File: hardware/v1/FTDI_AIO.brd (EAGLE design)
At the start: 49.5 x 49.5 mm, 45 parts, among them IC1 MCP1702-3.3, IC2 FT232RL, X1 ISP, X2 USB-A-H, X3 UART

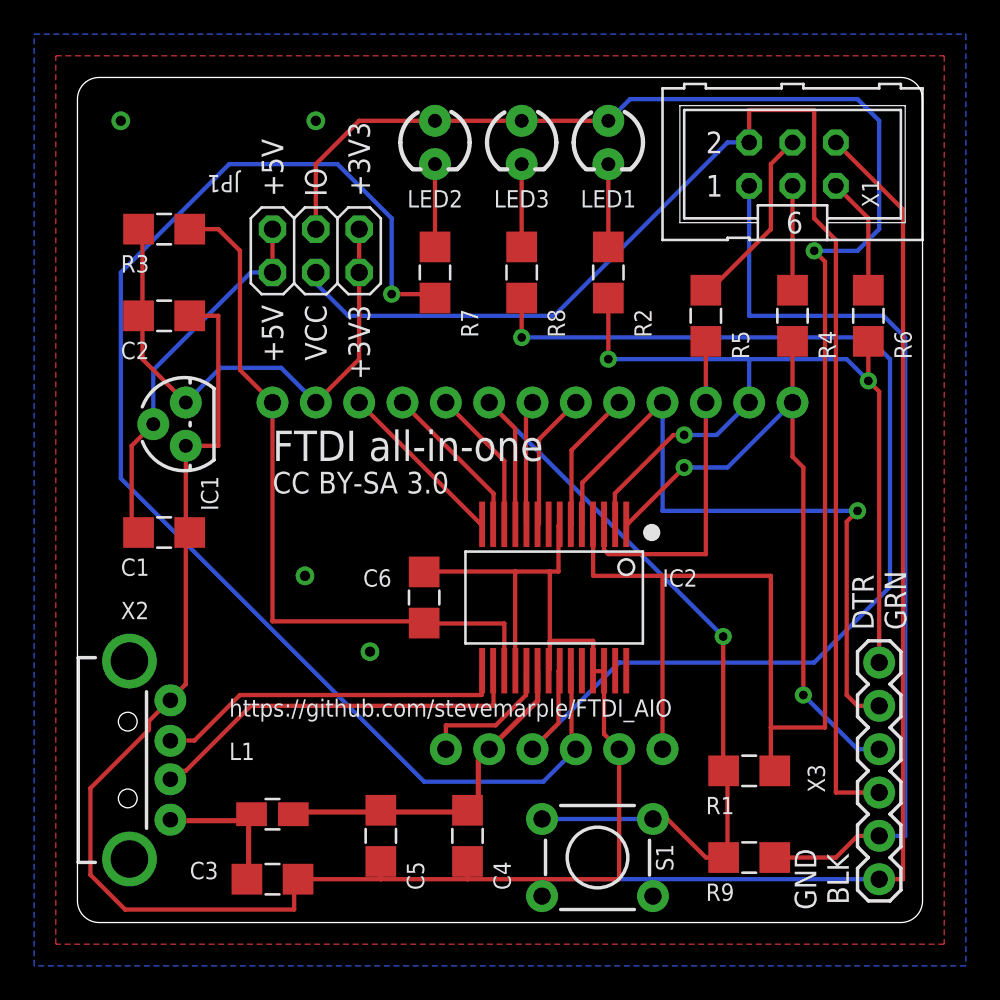
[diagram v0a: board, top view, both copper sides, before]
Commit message: Minor track and via changes.
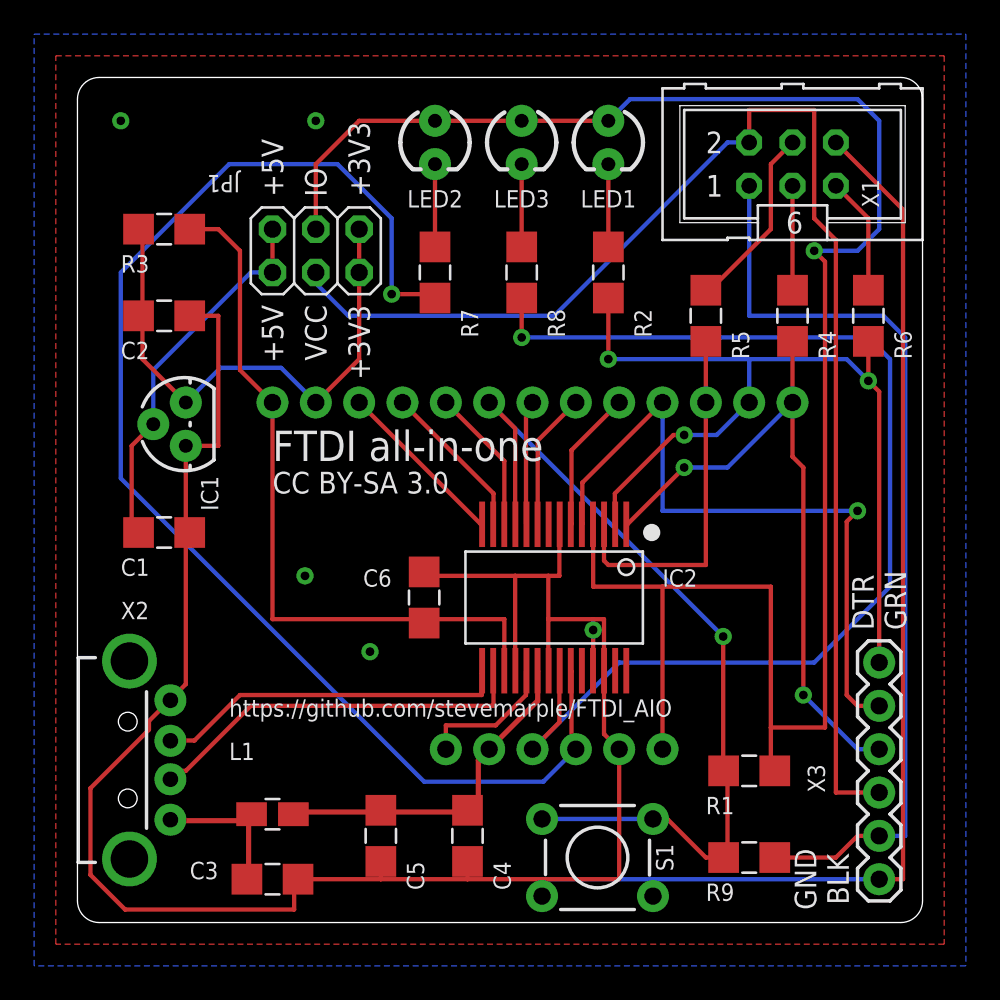
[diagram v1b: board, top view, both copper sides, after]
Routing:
- net GND: track 183.7 -> 188.1 mm, vias 4 -> 5
- net RTS: track 20.0 -> 21.3 mm
- net VCC: track 116.3 -> 115.6 mm
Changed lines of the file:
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@@
 <wire x1="46.99" y1="2.54" x2="48.387" y2="2.54" width="0.254" layer="1"/>
 <wire x1="6.477" y1="35.56" x2="6.579" y2="35.56" width="0.254" layer="1"/>
-<wire x1="28.194" y1="20.574" x2="27.686" y2="20.574" width="0.254" layer="1"/>
-<wire x1="27.686" y1="20.574" x2="25.654" y2="20.574" width="0.254" layer="1"/>
-<wire x1="25.654" y1="20.574" x2="20.32" y2="20.574" width="0.254" layer="1"/>
-<wire x1="28.194" y1="23.241" x2="28.194" y2="20.574" width="0.254" layer="1"/>
-<wire x1="20.32" y1="20.574" x2="20.32" y2="20.549" width="0.254" layer="1"/>
-<wire x1="28.194" y1="23.241" x2="28.265" y2="23.341" width="0.254" layer="1"/>
-<wire x1="25.654" y1="20.574" x2="25.654" y2="14.859" width="0.254" layer="1"/>
+<wire x1="28.2448" y1="20.32" x2="27.5971" y2="20.32" width="0.254" layer="1"/>
+<wire x1="27.5971" y1="20.32" x2="25.654" y2="20.32" width="0.254" layer="1"/>
+<wire x1="25.654" y1="20.32" x2="20.32" y2="20.32" width="0.254" layer="1"/>
+<wire x1="28.2448" y1="23.241" x2="28.2448" y2="20.32" width="0.254" layer="1"/>
+<wire x1="20.32" y1="20.32" x2="20.32" y2="20.549" width="0.254" layer="1"/>
+<wire x1="28.2448" y1="23.241" x2="28.265" y2="23.341" width="0.254" layer="1"/>
+<wire x1="25.654" y1="20.32" x2="25.654" y2="14.859" width="0.254" layer="1"/>
 <wire x1="25.654" y1="14.859" x2="25.665" y2="14.759" width="0.254" layer="1"/>
-<wire x1="27.686" y1="20.574" x2="27.686" y2="16.51" width="0.254" layer="1"/>
-<wire x1="27.686" y1="16.51" x2="27.686" y2="14.859" width="0.254" layer="1"/>
-<wire x1="27.686" y1="14.859" x2="27.615" y2="14.759" width="0.254" layer="1"/>
-<wire x1="30.861" y1="14.732" x2="30.226" y2="14.732" width="0.254" layer="1"/>
+<wire x1="27.5971" y1="20.32" x2="27.5971" y2="17.78" width="0.254" layer="1"/>
+<wire x1="27.5971" y1="17.78" x2="27.5971" y2="14.859" width="0.254" layer="1"/>
+<wire x1="27.5971" y1="14.859" x2="27.615" y2="14.759" width="0.254" layer="1"/>
 <wire x1="30.226" y1="14.732" x2="30.215" y2="14.759" width="0.254" layer="1"/>
 <wire x1="30.861" y1="14.732" x2="30.865" y2="14.759" width="0.254" layer="1"/>
@@
 <wire x1="31.75" y1="10.16" x2="30.861" y2="11.049" width="0.254" layer="1"/>
 <wire x1="30.861" y1="14.605" x2="30.865" y2="14.759" width="0.254" layer="1"/>
-<wire x1="30.226" y1="16.51" x2="27.686" y2="16.51" width="0.254" layer="1"/>
-<wire x1="30.226" y1="14.859" x2="30.226" y2="16.51" width="0.254" layer="1"/>
+<wire x1="30.226" y1="17.78" x2="27.5971" y2="17.78" width="0.254" layer="1"/>
+<wire x1="30.226" y1="14.859" x2="30.226" y2="17.78" width="0.254" layer="1"/>
 <wire x1="30.226" y1="14.859" x2="30.215" y2="14.759" width="0.254" layer="1"/>
 <wire x1="4.191" y1="11.811" x2="5.334" y2="12.954" width="0.254" layer="1"/>
@@
 <vertex x="-2.54" y="-2.54"/>
 </polygon>
-<via x="2.54" y="46.99" extent="1-16" drill="0.6"/>
-<via x="13.97" y="46.99" extent="1-16" drill="0.6"/>
-<via x="13.335" y="20.32" extent="1-16" drill="0.6"/>
-<via x="17.145" y="15.875" extent="1-16" drill="0.6"/>
+<via x="2.54" y="46.99" extent="1-16" drill="0.508"/>
+<via x="13.97" y="46.99" extent="1-16" drill="0.508"/>
+<via x="13.335" y="20.32" extent="1-16" drill="0.508"/>
+<via x="17.145" y="15.875" extent="1-16" drill="0.508"/>
+<via x="30.226" y="17.145" extent="1-16" drill="0.508"/>
+<wire x1="30.861" y1="14.732" x2="30.861" y2="17.78" width="0.254" layer="1"/>
+<wire x1="30.861" y1="17.78" x2="30.226" y2="17.78" width="0.254" layer="1"/>
 </signal>
 <signal name="TX">
@@
 <contactref element="JP1" pad="4"/>
 <contactref element="LED1" pad="A"/>
-<wire x1="40.64" y1="20.32" x2="40.64" y2="11.43" width="0.254" layer="1"/>
-<wire x1="34.29" y1="20.32" x2="40.64" y2="20.32" width="0.254" layer="1"/>
-<wire x1="34.29" y1="10.16" x2="34.29" y2="20.32" width="0.254" layer="1"/>
-<wire x1="30.226" y1="20.32" x2="30.226" y2="23.241" width="0.254" layer="1"/>
-<wire x1="34.29" y1="20.32" x2="30.226" y2="20.32" width="0.254" layer="1"/>
+<wire x1="40.64" y1="19.685" x2="40.64" y2="11.43" width="0.254" layer="1"/>
+<wire x1="34.29" y1="19.685" x2="40.64" y2="19.685" width="0.254" layer="1"/>
+<wire x1="34.29" y1="10.16" x2="34.29" y2="19.685" width="0.254" layer="1"/>
+<wire x1="30.226" y1="19.685" x2="30.226" y2="23.241" width="0.254" layer="1"/>
+<wire x1="34.29" y1="19.685" x2="30.226" y2="19.685" width="0.254" layer="1"/>
 <wire x1="30.226" y1="23.241" x2="30.215" y2="23.341" width="0.254" layer="1"/>
 <wire x1="16.51" y1="46.99" x2="13.97" y2="44.45" width="0.254" layer="1"/>
@@
 <wire x1="31.75" y1="15.24" x2="43.18" y2="15.24" width="0.254" layer="16"/>
 <wire x1="26.67" y1="10.16" x2="31.75" y2="15.24" width="0.254" layer="16"/>
-<wire x1="28.194" y1="11.684" x2="28.194" y2="14.732" width="0.254" layer="1"/>
-<wire x1="26.67" y1="10.16" x2="28.194" y2="11.684" width="0.254" layer="1"/>
-<wire x1="28.194" y1="14.732" x2="28.265" y2="14.759" width="0.254" layer="1"/>
+<wire x1="28.2448" y1="11.7348" x2="28.2448" y2="14.732" width="0.254" layer="1"/>
+<wire x1="26.67" y1="10.16" x2="28.2448" y2="11.7348" width="0.254" layer="1"/>
+<wire x1="28.2448" y1="14.732" x2="28.265" y2="14.759" width="0.254" layer="1"/>
 <via x="26.035" y="34.29" extent="1-16" drill="0.508"/>
 </signal>
@@
 <contactref element="C6" pad="1"/>
 <contactref element="U$6" pad="1"/>
-<wire x1="25.019" y1="17.526" x2="20.32" y2="17.526" width="0.254" layer="1"/>
-<wire x1="25.019" y1="14.859" x2="25.019" y2="17.526" width="0.254" layer="1"/>
-<wire x1="20.32" y1="17.526" x2="20.32" y2="17.551" width="0.254" layer="1"/>
+<wire x1="25.019" y1="17.78" x2="20.32" y2="17.78" width="0.254" layer="1"/>
+<wire x1="25.019" y1="14.859" x2="25.019" y2="17.78" width="0.254" layer="1"/>
 <wire x1="25.019" y1="14.859" x2="25.015" y2="14.759" width="0.254" layer="1"/>
 <wire x1="9.525" y1="39.37" x2="8.255" y2="40.64" width="0.254" layer="1"/>
@@
 <wire x1="9.525" y1="32.385" x2="9.525" y2="39.37" width="0.254" layer="1"/>
 <wire x1="11.43" y1="30.48" x2="9.525" y2="32.385" width="0.254" layer="1"/>
-<wire x1="11.43" y1="17.653" x2="20.32" y2="17.653" width="0.254" layer="1"/>
-<wire x1="11.43" y1="30.48" x2="11.43" y2="17.653" width="0.254" layer="1"/>
-<wire x1="20.32" y1="17.653" x2="20.32" y2="17.551" width="0.254" layer="1"/>
+<wire x1="11.43" y1="17.78" x2="20.32" y2="17.78" width="0.254" layer="1"/>
+<wire x1="11.43" y1="30.48" x2="11.43" y2="17.78" width="0.254" layer="1"/>
+<wire x1="20.32" y1="17.78" x2="20.32" y2="17.551" width="0.254" layer="1"/>
 </signal>
 <signal name="N$14">
 <contactref element="IC2" pad="9"/>
 <contactref element="U$10" pad="1"/>
-<wire x1="27.051" y1="28.321" x2="27.051" y2="23.368" width="0.254" layer="1"/>
-<wire x1="29.21" y1="30.48" x2="27.051" y2="28.321" width="0.254" layer="1"/>
-<wire x1="27.051" y1="23.368" x2="26.965" y2="23.341" width="0.254" layer="1"/>
+<wire x1="26.9748" y1="28.2448" x2="26.9748" y2="23.368" width="0.254" layer="1"/>
+<wire x1="29.21" y1="30.48" x2="26.9748" y2="28.2448" width="0.254" layer="1"/>
+<wire x1="26.9748" y1="23.368" x2="26.965" y2="23.341" width="0.254" layer="1"/>
 </signal>
 <signal name="N$21">
@@
 <contactref element="R5" pad="2"/>
 <wire x1="36.83" y1="30.48" x2="36.83" y2="34.061" width="0.254" layer="1"/>
-<wire x1="30.861" y1="21.844" x2="30.861" y2="23.241" width="0.254" layer="1"/>
-<wire x1="31.115" y1="21.59" x2="30.861" y2="21.844" width="0.254" layer="1"/>
-<wire x1="36.83" y1="21.59" x2="31.115" y2="21.59" width="0.254" layer="1"/>
-<wire x1="36.83" y1="30.48" x2="36.83" y2="21.59" width="0.254" layer="1"/>
+<wire x1="30.861" y1="21.209" x2="30.861" y2="23.241" width="0.254" layer="1"/>
+<wire x1="31.115" y1="20.955" x2="30.861" y2="21.209" width="0.254" layer="1"/>
+<wire x1="36.83" y1="20.955" x2="31.115" y2="20.955" width="0.254" layer="1"/>
+<wire x1="36.83" y1="30.48" x2="36.83" y2="20.955" width="0.254" layer="1"/>
 <wire x1="30.861" y1="23.241" x2="30.865" y2="23.341" width="0.254" layer="1"/>
 </signal>

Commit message: Updating to use modified FT232R package. Rerouted TXLED.
TXLED signal rerouted to avoid breaking ground place in vicinity of
USB data lines.
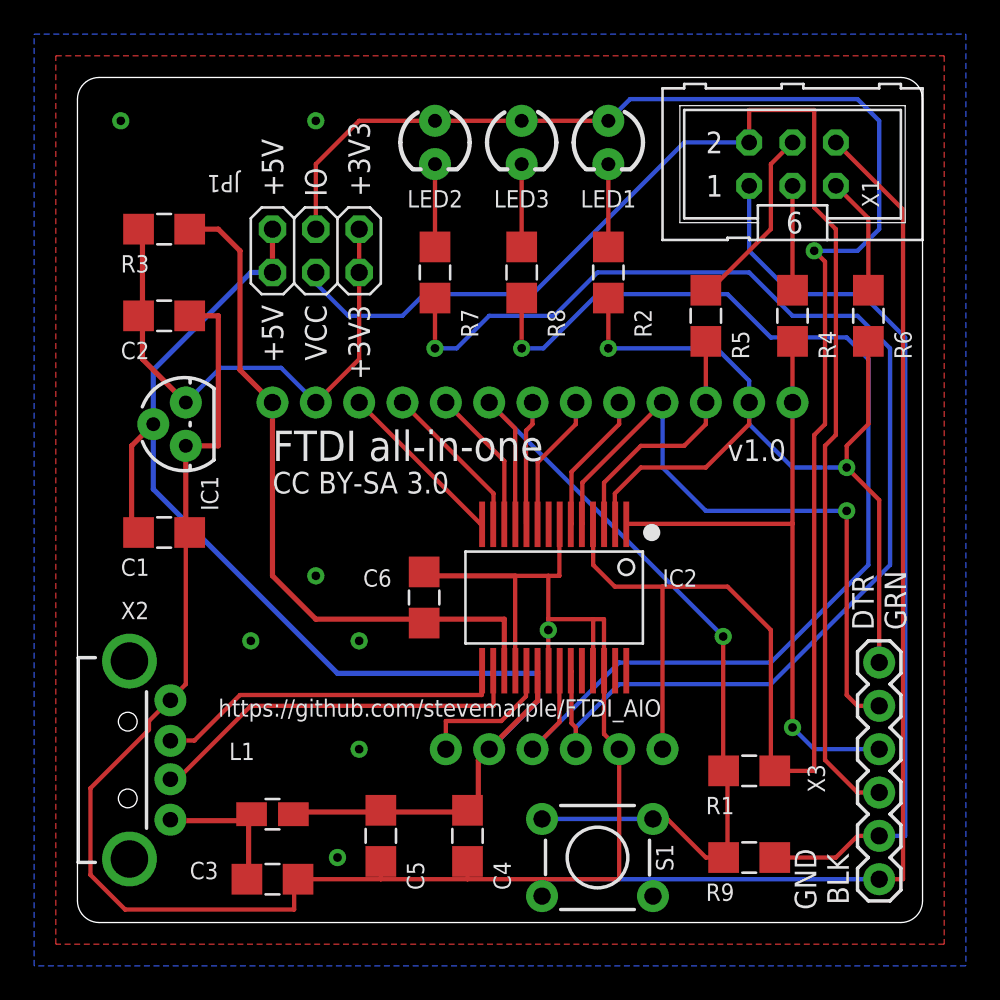
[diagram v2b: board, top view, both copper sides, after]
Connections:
- net N$11 renamed TXLED
- net N$12 renamed RXLED
- net N$26 renamed !RESET
- removed net +5V: C1.1, IC1.2, JP1.1, JP1.2
- removed net VUSB_FILT: C4.1, C5.1, IC2.20, L1.2, U$4.1
- new net VBUS_FILT: C1.1, C4.1, C5.1, IC1.2, IC2.20, JP1.1, JP1.2, L1.2, U$4.1
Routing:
- net VBUS_FILT: track 0.00 -> 79.5 mm
- net +5V: track 22.5 -> 0.00 mm
- net VUSB_FILT: track 20.7 -> 0.00 mm
- net RTS: track 21.3 -> 14.7 mm
- net TXLED: track 78.6 -> 74.6 mm
- net RX: track 40.1 -> 37.7 mm
- net CTS_PROT: track 54.7 -> 52.4 mm
- net 3V3_OUT: track 42.7 -> 41.2 mm
- net TX: track 39.4 -> 38.0 mm, vias 2 -> 1
- net DTR: track 56.6 -> 57.8 mm, vias 3 -> 2
- net GND: track 188.1 -> 188.3 mm, vias 5 -> 8
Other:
- board text added: "v1.0"

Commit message: Swapping capcitor positions for better decoupling.
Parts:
- moved C4 5.08 mm to (17.8, 5.08)
- moved C5 5.08 mm to (22.9, 5.08)
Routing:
- net VBUS_FILT: track 79.5 -> 80.4 mm
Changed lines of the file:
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@@
 <element name="U$18" library="SteveMarple" package="PAD" value="PAD" x="31.75" y="10.16" smashed="yes" rot="R90"/>
 <element name="U$13" library="SteveMarple" package="PAD" value="PAD" x="21.59" y="10.16" smashed="yes" rot="R90"/>
-<element name="C5" library="SteveMarple" package="1206-HAND" value="100n" x="17.78" y="5.08" smashed="yes" rot="R270">
+<element name="C5" library="SteveMarple" package="1206-HAND" value="100n" x="22.86" y="5.08" smashed="yes" rot="R270">
+<attribute name="NAME" x="25.4" y="1.905" size="1.016" layer="25" ratio="10" rot="R90"/>
+<attribute name="VALUE" x="25.4" y="5.08" size="1.016" layer="27" ratio="10" rot="R90"/>
+</element>
+<element name="C4" library="SteveMarple" package="1206-HAND" value="4u7" x="17.78" y="5.08" smashed="yes" rot="R270">
 <attribute name="NAME" x="20.32" y="1.905" size="1.016" layer="25" ratio="10" rot="R90"/>
 <attribute name="VALUE" x="20.32" y="5.08" size="1.016" layer="27" ratio="10" rot="R90"/>
-</element>
-<element name="C4" library="SteveMarple" package="1206-HAND" value="4u7" x="22.86" y="5.08" smashed="yes" rot="R270">
-<attribute name="NAME" x="25.4" y="1.905" size="1.016" layer="25" ratio="10" rot="R90"/>
-<attribute name="VALUE" x="25.4" y="5.08" size="1.016" layer="27" ratio="10" rot="R90"/>
 </element>
 <element name="C3" library="SteveMarple" package="1206-HAND" value="10n" x="11.43" y="2.54" smashed="yes">
@@
 <wire x1="12.7" y1="2.54" x2="12.7" y2="0.762" width="0.254" layer="1"/>
 <wire x1="5.334" y1="12.954" x2="5.448" y2="13.025" width="0.254" layer="1"/>
+<wire x1="27.2288" y1="2.54" x2="22.86" y2="2.54" width="0.254" layer="1"/>
 <wire x1="22.86" y1="2.54" x2="17.78" y2="2.54" width="0.254" layer="1"/>
-<wire x1="12.929" y1="2.54" x2="17.78" y2="2.54" width="0.254" layer="1"/>
-<wire x1="17.78" y1="2.54" x2="17.78" y2="3.581" width="0.254" layer="1"/>
+<wire x1="17.78" y1="2.54" x2="12.929" y2="2.54" width="0.254" layer="1"/>
 <wire x1="12.7" y1="2.54" x2="12.929" y2="2.54" width="0.254" layer="1"/>
-<wire x1="22.86" y1="2.54" x2="22.86" y2="3.581" width="0.254" layer="1"/>
 <wire x1="6.35" y1="22.987" x2="6.477" y2="22.86" width="0.254" layer="1"/>
 <wire x1="6.35" y1="27.94" x2="6.35" y2="22.987" width="0.3048" layer="1"/>
@@
 <wire x1="27.2288" y1="2.54" x2="27.2288" y2="1.5494" width="0.254" layer="16"/>
 <wire x1="33.7312" y1="1.5494" x2="33.7312" y2="2.54" width="0.254" layer="16"/>
-<wire x1="22.86" y1="2.54" x2="27.2288" y2="2.54" width="0.254" layer="1"/>
 <wire x1="27.2288" y1="2.54" x2="27.2288" y2="1.5494" width="0.254" layer="1"/>
 <wire x1="31.75" y1="10.16" x2="31.75" y2="2.54" width="0.254" layer="1"/>
@@
 <via x="10.16" y="16.51" extent="1-16" drill="0.508"/>
 <via x="15.24" y="3.81" extent="1-16" drill="0.508"/>
+<wire x1="17.78" y1="3.581" x2="17.78" y2="2.54" width="0.254" layer="1"/>
+<wire x1="22.86" y1="3.581" x2="22.86" y2="2.54" width="0.254" layer="1"/>
 </signal>
 <signal name="TX">
@@
 <wire x1="24.13" y1="10.16" x2="26.9748" y2="13.0048" width="0.3048" layer="1"/>
 <wire x1="26.9748" y1="14.732" x2="26.965" y2="14.759" width="0.3048" layer="1"/>
-<wire x1="17.78" y1="6.477" x2="13.335" y2="6.477" width="0.3048" layer="1"/>
 <wire x1="13.335" y1="6.477" x2="12.7" y2="6.35" width="0.3048" layer="1"/>
 <wire x1="12.7" y1="6.35" x2="12.655" y2="6.35" width="0.3048" layer="1"/>
+<wire x1="13.335" y1="6.477" x2="17.78" y2="6.477" width="0.3048" layer="1"/>
 <wire x1="17.78" y1="6.477" x2="22.86" y2="6.477" width="0.3048" layer="1"/>
-<wire x1="17.78" y1="6.477" x2="17.78" y2="6.579" width="0.3048" layer="1"/>
 <wire x1="23.495" y1="9.525" x2="24.13" y2="10.16" width="0.3048" layer="1"/>
-<wire x1="22.86" y1="6.579" x2="23.495" y2="6.604" width="0.3048" layer="1"/>
 <wire x1="23.495" y1="6.604" x2="23.495" y2="9.525" width="0.3048" layer="1"/>
-<wire x1="22.86" y1="6.477" x2="22.86" y2="6.579" width="0.3048" layer="1"/>
 <contactref element="JP1" pad="1"/>
 <contactref element="JP1" pad="2"/>
@@
 <wire x1="26.9748" y1="14.605" x2="26.9748" y2="13.0048" width="0.3048" layer="16"/>
 <wire x1="26.9748" y1="13.0048" x2="24.13" y2="10.16" width="0.3048" layer="16"/>
+<wire x1="22.86" y1="6.579" x2="22.86" y2="6.477" width="0.3048" layer="1"/>
+<wire x1="23.495" y1="6.604" x2="22.86" y2="6.604" width="0.3048" layer="1"/>
+<wire x1="22.86" y1="6.604" x2="22.86" y2="6.579" width="0.3048" layer="1"/>
+<wire x1="17.78" y1="6.579" x2="17.78" y2="6.477" width="0.3048" layer="1"/>
+<wire x1="13.335" y1="6.477" x2="12.655" y2="6.477" width="0.3048" layer="1"/>
+<wire x1="12.655" y1="6.477" x2="12.655" y2="6.35" width="0.3048" layer="1"/>
 </signal>
 <signal name="VUSB" class="2">
